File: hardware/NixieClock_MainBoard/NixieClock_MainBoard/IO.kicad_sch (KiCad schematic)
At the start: 1 part, among them U4 PCA9547D

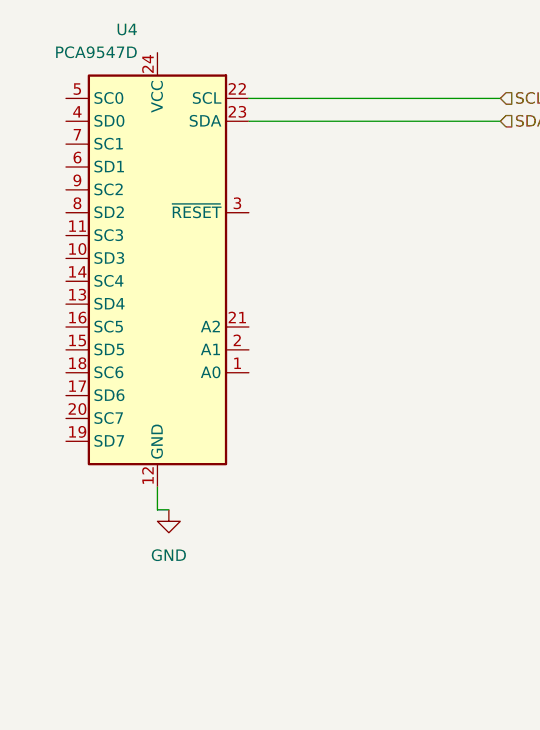
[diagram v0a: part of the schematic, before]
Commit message: update pcb. distance between fpc-connector corrected
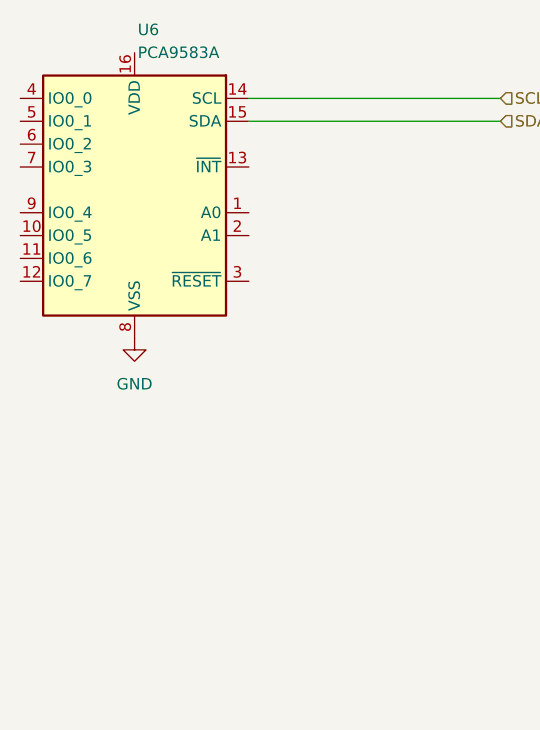
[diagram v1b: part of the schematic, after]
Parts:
- removed U4: PCA9547D, Package_SO:SOIC-24W_7.5x15.4mm_P1.27mm, symbol Interface_Expansion:PCA9547D
- added U6: PCA9583A, Package_DFN_QFN:HVQFN-16-1EP_3x3mm_P0.5mm_EP1.5x1.5mm, symbol ownSymbols:PCA9538ABS
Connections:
- net GND: now also U6.8 (VSS)
- net SCL: now also U6.14 (SCL)
- net SDA: now also U6.15 (SDA)
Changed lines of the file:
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@@
-	(wire
-		(pts
-			(xy 90.17 99.06) (xy 91.44 99.06)
-		)
-		(stroke
-			(width 0)
-			(type default)
-		)
-	)
 	(wire
 		(pts
@@
 		(pts
 			(xy 100.33 53.34) (xy 128.27 53.34)
-		)
-		(stroke
-			(width 0)
-			(type default)
-		)
-	)
-	(wire
-		(pts
-			(xy 90.17 96.52) (xy 90.17 99.06)
 		)
 		(stroke
@@
 	)
 	(symbol
-		(lib_id "Interface_Expansion:PCA9547D")
-		(at 90.17 71.12 0)
+		(lib_id "ownSymbols:PCA9538ABS")
+		(at 87.63 63.5 0)
 		(mirror y)
 		(unit 1)
@@
 		(on_board yes)
 		(dnp no)
-		(property "Reference" "U4"
+		(fields_autoplaced yes)
+		(property "Reference" "U6"
 			(at 87.9759 45.72 0)
 			(effects
@@
 					(size 1.27 1.27)
 				)
-				(justify left)
+				(justify right)
 			)
 		)
-		(property "Value" "PCA9547D"
+		(property "Value" "PCA9583A"
 			(at 87.9759 48.26 0)
 			(effects
@@
 					(size 1.27 1.27)
 				)
-				(justify left)
+				(justify right)
 			)
 		)
-		(property "Footprint" "Package_SO:SOIC-24W_7.5x15.4mm_P1.27mm"
-			(at 90.17 96.52 0)
+		(property "Footprint" "Package_DFN_QFN:HVQFN-16-1EP_3x3mm_P0.5mm_EP1.5x1.5mm"
+			(at 87.63 64.516 0)
 			(effects
 				(font
@@
 			)
 		)
-		(property "Datasheet" "https://www.nxp.com/docs/en/data-sheet/PCA9547.pdf"
-			(at 88.9 64.77 0)
+		(property "Datasheet" "https://www.nxp.com/docs/en/data-sheet/PCA9538A.pdf"
+			(at 88.138 66.04 0)
 			(effects
 				(font
@@
 			)
 		)
-		(property "Description" "Low voltage 8-channel I2C switch with reset, SO-24"
-			(at 90.17 71.12 0)
+		(property "Description" "Low-voltage 8-bit I2C-bus I/O port with interrupt and reset"
+			(at 87.63 62.23 0)
 			(effects
 				(font
@@
 			)
 		)
-		(pin "12"
+		(pin "14"
 		)
-		(pin "22"
+		(pin "7"
 		)
-		(pin "23"
-		)
-		(pin "6"
+		(pin "1"
 		)
 		(pin "8"
 		)
-		(pin "14"
+		(pin "11"
+		)
+		(pin "13"
+		)
+		(pin "16"
 		)
 		(pin "2"
 		)
-		(pin "13"
-		)
-		(pin "11"
-		)
-		(pin "17"
-		)
-		(pin "21"
-		)
-		(pin "24"
+		(pin "15"
 		)
 		(pin "3"
@@
 		(pin "5"
 		)
-		(pin "19"
+		(pin "6"
+		)
+		(pin "4"
+		)
+		(pin "10"
 		)
 		(pin "9"
 		)
-		(pin "20"
-		)
-		(pin "16"
-		)
-		(pin "18"
-		)
-		(pin "7"
-		)
-		(pin "10"
-		)
-		(pin "1"
-		)
-		(pin "15"
-		)
-		(pin "4"
+		(pin "12"
 		)
 		(instances
 			(project "NixieClock_MainBoard"
 				(path "/5ddb5910-d1ea-4e23-971a-19156fc3bbe9/079c23e2-2395-4de4-8770-a54833c4570a"
-					(reference "U4")
+					(reference "U6")
 					(unit 1)
 				)
@@
 	(symbol
 		(lib_id "power:GND")
-		(at 91.44 99.06 0)
+		(at 87.63 80.01 0)
 		(unit 1)
 		(exclude_from_sim no)
@@
 		(fields_autoplaced yes)
 		(property "Reference" "#PWR06"
-			(at 91.44 105.41 0)
+			(at 87.63 86.36 0)
 			(effects
 				(font
@@
 		)
 		(property "Value" "GND"
-			(at 91.44 104.14 0)
+			(at 87.63 85.09 0)
 			(effects
 				(font
@@
 		)
 		(property "Footprint" ""
-			(at 91.44 99.06 0)
+			(at 87.63 80.01 0)
 			(effects
 				(font
@@
 		)
 		(property "Datasheet" ""
-			(at 91.44 99.06 0)
+			(at 87.63 80.01 0)
 			(effects
 				(font
@@
 		)
 		(property "Description" "Power symbol creates a global label with name \"GND\" , ground"
-			(at 91.44 99.06 0)
+			(at 87.63 80.01 0)
 			(effects
 				(font

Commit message: layout mainboard
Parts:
- added C10: 1u0, Capacitor_SMD:C_0603_1608Metric, symbol Device:C
- added C9: 100nF, Capacitor_SMD:C_0603_1608Metric, symbol Device:C
- added J8: Conn_01x08, Connector_PinHeader_2.54mm:PinHeader_1x08_P2.54mm_Vertical, symbol Connector_Generic:Conn_01x08
- added J9: Conn_01x03, Connector_PinHeader_2.54mm:PinHeader_1x03_P2.54mm_Vertical, symbol Connector_Generic:Conn_01x03
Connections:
- net GND: now also U6.1 (A0), U6.2 (A1), C10.2, C9.2, J8.2 (Pin_2)
- net at U6.10 (IO0_5): now also J8.8 (Pin_8)
- net ~{INT_IO}: now reaches U6.13 (~{INT})
- net +3.3V: now reaches U6.16 (VDD)
- net +3.3V: now also U6.3 (~{RESET}), C10.1, C9.1, J8.1 (Pin_1)
- net at U6.4 (IO0_0): now also J8.3 (Pin_3)
- net at U6.5 (IO0_1): now also J8.4 (Pin_4)
- net at U6.6 (IO0_2): now also J8.5 (Pin_5)
- net at U6.7 (IO0_3): now also J8.6 (Pin_6)
- net at U6.9 (IO0_4): now also J8.7 (Pin_7)
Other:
- moved on the sheet: U6

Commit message: update mainboard
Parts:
- added C11: 100nF, Capacitor_SMD:C_0603_1608Metric, symbol Device:C
- added JP1: SolderJumper_3_Open, Jumper:SolderJumper-3_P1.3mm_Open_Pad1.0x1.5mm, symbol Jumper:SolderJumper_3_Open
- added U13: NC7SZ125M5X, Package_TO_SOT_SMD:SOT-23-5, symbol 74xGxx:NC7SZ125M5X
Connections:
- net +3.3V: now also C11.1, JP1.3 (B), U13.1 (~{OE}), U13.5 (VCC)
- net GND: now also J9.3 (Pin_3), C11.2, U13.3 (GND)
- net WS28XX: now also U13.2 (A)
- net at J9.1 (Pin_1): now also JP1.2 (C)
- net at J9.2 (Pin_2): now also U13.4 (Y)
- new net +5V: JP1.1 (A)
